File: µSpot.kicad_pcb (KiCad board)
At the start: 2 copper layers, 80 x 35 mm, 54 parts, among them J1 Conn_01x03, Q1 PSMN0R9-30YLD, Q2 PSMN0R9-30YLD, Q3 PSMN0R9-30YLD, Q4 PSMN0R9-30YLD, Q5 PSMN0R9-30YLD, Q6 PSMN0R9-30YLD, SW1 Rotary_Encoder_Switch, U1 AP65211A, U2 MIC5365-3.3YD5, U3 ATtiny406-S, U4 OLED_Display_9616, U5 FAN3111

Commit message: Layout finish
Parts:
- removed C10, C11: 1u, Capacitor_SMD:C_1206_3216Metric_Pad1.42x1.75mm_HandSolder
- added D1: Red, LED_SMD:LED_0805_2012Metric_Pad1.15x1.40mm_HandSolder, F.Cu at (145.7, 91.9)
- added D2: 2SS100L-W, Diode_SMD:D_SOD-123F, F.Cu at (147.6, 109.3)
- added D6: BZX84C3V3, Package_TO_SOT_SMD:SOT-23, F.Cu at (136.7, 90.3)
- added D7: BZX84C3V3, Package_TO_SOT_SMD:SOT-23, F.Cu at (141.0, 97.3)
- added J2: Conn_01x04, Connector_PinSocket_2.54mm:PinSocket_1x04_P2.54mm_Vertical_SMD_Pin1Left, F.Cu at (153.7, 85.7)
- added Q7: Q_PMOS_DGS, Package_TO_SOT_SMD:SOT-23, F.Cu at (149.0, 106.2)
- added R14: 5k, Resistor_SMD:R_0805_2012Metric_Pad1.15x1.40mm_HandSolder, F.Cu at (133.7, 92.3)
- added R22: 1k8, Resistor_SMD:R_0805_2012Metric_Pad1.15x1.40mm_HandSolder, F.Cu at (136.7, 93.2)
- added R23: 5k, Resistor_SMD:R_0805_2012Metric_Pad1.15x1.40mm_HandSolder, F.Cu at (138.0, 99.2)
- added R24: 1k8, Resistor_SMD:R_0805_2012Metric_Pad1.15x1.40mm_HandSolder, F.Cu at (141.1, 100.0)
- C1, C5: footprint Capacitor_SMD:C_1206_3216Metric_Pad1.42x1.75mm_HandSolder -> Capacitor_SMD:C_0805_2012Metric_Pad1.18x1.45mm_HandSolder
- C12, C2, C3, C4, C6: footprint Capacitor_SMD:C_1206_3216Metric_Pad1.42x1.75mm_HandSolder -> Capacitor_SMD:C_0805_2012Metric_Pad1.15x1.40mm_HandSolder
- C7, C8: value 1u -> 1n; footprint Capacitor_SMD:C_1206_3216Metric_Pad1.42x1.75mm_HandSolder -> Capacitor_SMD:C_0805_2012Metric_Pad1.15x1.40mm_HandSolder
- C9: value 1u -> 3.3u; footprint Capacitor_SMD:C_1206_3216Metric_Pad1.42x1.75mm_HandSolder -> Capacitor_SMD:C_0805_2012Metric_Pad1.15x1.40mm_HandSolder
- D3, D4: footprint LED_SMD:LED_1206_3216Metric_Pad1.42x1.75mm_HandSolder -> LED_SMD:LED_0805_2012Metric_Pad1.15x1.40mm_HandSolder
- L1: footprint Inductor_SMD:L_Taiyo-Yuden_MD-2020 -> Inductor_SMD:L_0805_2012Metric_Pad1.15x1.40mm_HandSolder
- R1, R3: value 4k7 -> 10k; footprint Resistor_SMD:R_1206_3216Metric_Pad1.42x1.75mm_HandSolder -> Resistor_SMD:R_0805_2012Metric_Pad1.15x1.40mm_HandSolder
- R10: value 390k -> 10k; footprint Resistor_SMD:R_1206_3216Metric_Pad1.42x1.75mm_HandSolder -> Resistor_SMD:R_0805_2012Metric_Pad1.15x1.40mm_HandSolder
- R11: value 10k -> 100k; footprint Resistor_SMD:R_1206_3216Metric_Pad1.42x1.75mm_HandSolder -> Resistor_SMD:R_0805_2012Metric_Pad1.20x1.40mm_HandSolder
- R12: value 10k -> 5k; footprint Resistor_SMD:R_1206_3216Metric_Pad1.42x1.75mm_HandSolder -> Resistor_SMD:R_0805_2012Metric_Pad1.15x1.40mm_HandSolder
- R13, R15, R16, R17, R18, R19, R2, R20, R21, R4, R5, R6, R7, R8, R9, TH1: footprint Resistor_SMD:R_1206_3216Metric_Pad1.42x1.75mm_HandSolder -> Resistor_SMD:R_0805_2012Metric_Pad1.15x1.40mm_HandSolder
- U1: value AP65211A -> AP65111AWU; footprint Package_TO_SOT_SMD:TSOT-23-6_HandSoldering -> Package_TO_SOT_SMD:TSOT-23-6
- U3: value ATtiny406-S -> ATtiny404-SS; footprint Package_SO:SOIC-20W_7.5x12.8mm_P1.27mm -> Package_SO:SOIC-14_3.9x8.7mm_P1.27mm
- U4: value OLED_Display_9616 -> FAN3111E; footprint µSpot:OLED_Display_9616 -> Package_TO_SOT_SMD:SOT-23-5_HandSoldering
- U5: value FAN3111 -> ADS7029; footprint Package_TO_SOT_SMD:SOT-23-5_HandSoldering -> Package_SO:VSSOP-8_2.3x2mm_P0.5mm
- moved U4 40.5 mm to (108.5, 83.0)
- moved R12 31.4 mm to (164.3, 92.1)
- moved U5 31.2 mm to (134.0, 101.0)
- moved C12 30.7 mm to (166.4, 92.1)
- moved D5 30.7 mm to (171.9, 91.6)
- moved R13 30.7 mm to (168.9, 92.1)
- moved R11 25.0 mm to (143.8, 107.0), turned to 90 degrees
- moved C8 23.6 mm to (141.1, 102.1), turned to 0 degrees
- moved C7 22.6 mm to (136.7, 95.2), turned to 0 degrees
- moved C9 19.6 mm to (134.0, 97.6), turned to 0 degrees
- moved D4 18.4 mm to (141.5, 91.9), turned to 90 degrees
- moved R3 17.1 mm to (143.6, 91.9), turned to 90 degrees
- moved R10 16.3 mm to (157.3, 99.2)
- moved R8 8.84 mm to (129.7, 108.1), turned to 90 degrees
- moved C2 7.93 mm to (150.4, 101.6)
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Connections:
- C5 pad 1: +5V -> +5VA
- C7 pad 1: GND -> /WELD+
- C7 pad 2: Net-(C7-Pad2) -> GND
- C8 pad 1: GND -> /WELD-
- C8 pad 2: Net-(C8-Pad2) -> GND
- C9 pad 1: Net-(C9-Pad1) -> +3V3
- C9 pad 2: Net-(C9-Pad2) -> GND
- J1 pad 1: UDPI -> GND
- J1 pad 2: GND -> /UDPI
- J1 pad 3: +5V -> +5VP
- L1 pad 2: +5V -> +5VA
- R1 pad 1: ON_LED -> /TRIGGER
- R10 pad 1: Net-(R10-Pad1) -> +5VA
- R10 pad 2: GND -> Net-(D1-Pad2)
- R11 pad 1: +3V3 -> +5VP
- R11 pad 2: Net-(R11-Pad2) -> GND
- R4 pad 1: +5V -> +5VA
- R6 pad 2: CLK -> /CLK
- R7 pad 2: DT -> /DT
- R8 pad 2: SDA -> /SCL
- R9 pad 2: SCL -> /SDA
- SW1 pad A: CLK -> /CLK
- SW1 pad B: DT -> /DT
- SW1 pad S1: SWITCH -> /SWITCH
- U1 pad 1: GND -> +BATT
- U1 pad 2: (no net) -> GND
- U1 pad 3: +BATT -> Net-(C4-Pad2)
- U1 pad 4: Net-(R2-Pad2) -> Net-(C4-Pad1)
- U1 pad 6: Net-(C4-Pad1) -> Net-(R2-Pad2)
- U3 pad 10: SDA -> /UDPI
- U3 pad 11: SCL -> /WELD_CS
- U3 pad 12: Net-(U3-Pad12) -> /WELD_ADC
- U3 pad 13: Net-(U3-Pad13) -> /SCLK
- U3 pad 14: Net-(U3-Pad14) -> GND
- U3 pad 2: /TRIGGER -> /BAT_VOL
- U3 pad 3: ON_LED -> /TEMP
- U3 pad 4: Net-(U3-Pad4) -> /TRIGGER
- U3 pad 5: Net-(U3-Pad5) -> /SWITCH
- U3 pad 6: /TEMP -> /CLK
- U3 pad 7: SWITCH -> /DT
- U3 pad 8: CLK -> /SDA
- U3 pad 9: DT -> /SCL
- U4 pad 1: Net-(C9-Pad1) -> +5V
- U4 pad 2: Net-(C9-Pad2) -> GND
- U4 pad 3: Net-(C11-Pad1) -> /TRIGGER
- U4 pad 4: Net-(C11-Pad2) -> GND
- U4 pad 5: +3V3 -> /Welding/G
- U5 pad 1: +5V -> Net-(U5-Pad1)
- U5 pad 2: GND -> /SCLK
- U5 pad 3: /TRIGGER -> /WELD_ADC
- U5 pad 4: GND -> /WELD_CS
- U5 pad 5: /Welding/G -> /WELD-
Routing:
- net +5V: track 148.3 -> 94.5 mm, vias 2 -> 0
- net /SDA: track 0.00 -> 53.1 mm
- net /BAT_VOL: track 20.0 -> 72.0 mm, vias 0 -> 2
- net SDA: track 48.9 -> 0.00 mm
- net /SCL: track 0.00 -> 48.7 mm
- net SCL: track 48.2 -> 0.00 mm
- net /SWITCH: track 0.00 -> 39.1 mm
- net /CLK: track 0.00 -> 37.3 mm
- net ON_LED: track 30.4 -> 0.00 mm
- net /TRIGGER: track 22.9 -> 53.1 mm
- net SWITCH: track 28.3 -> 0.00 mm
- net +5VA: track 0.00 -> 26.8 mm
- net /DT: track 0.00 -> 26.6 mm
- net +5VP: track 0.00 -> 24.1 mm, vias 0 -> 2
- net CLK: track 22.4 -> 0.00 mm
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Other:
- board text added: "JLCJLCJLC"
- board text added: "Negative"
- board text added: "Positive"
- board text added: "Viking Elabs"

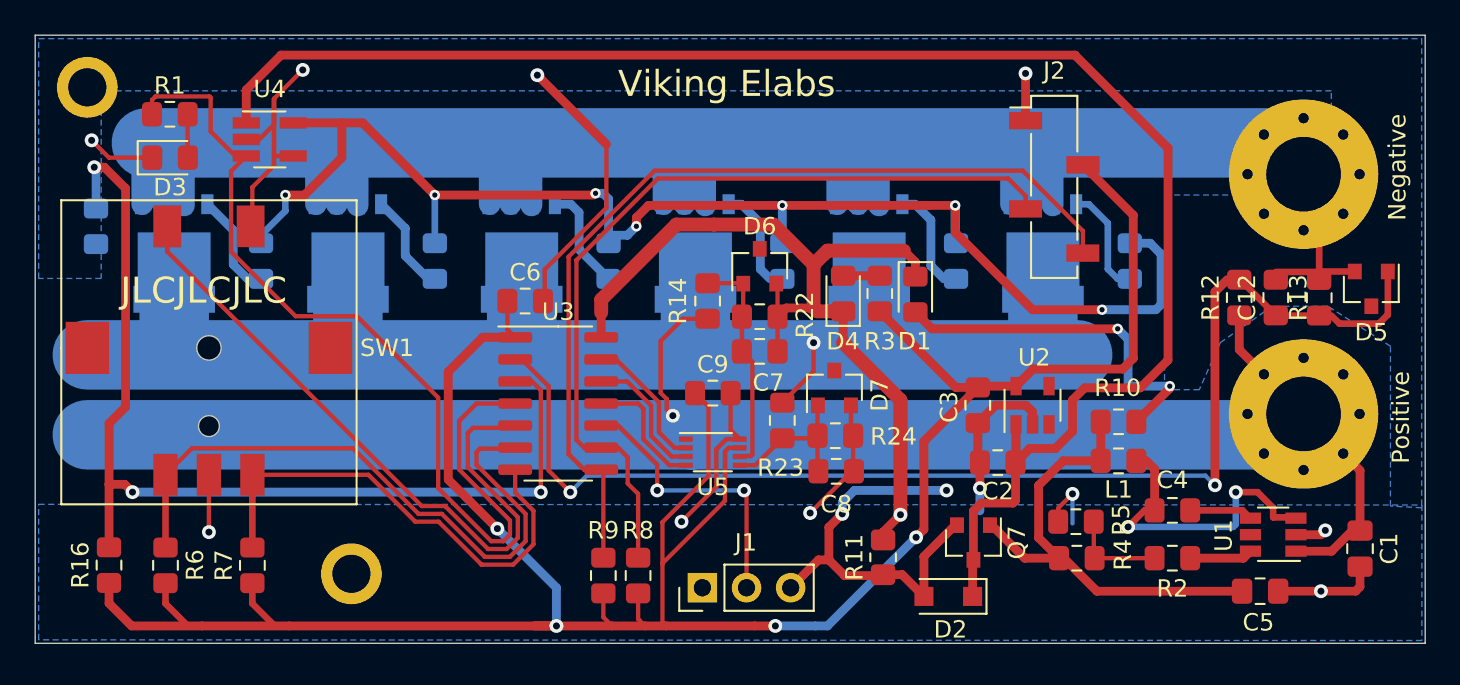
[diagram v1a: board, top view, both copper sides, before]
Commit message: Changes FAN3111 footprint and removed 5V
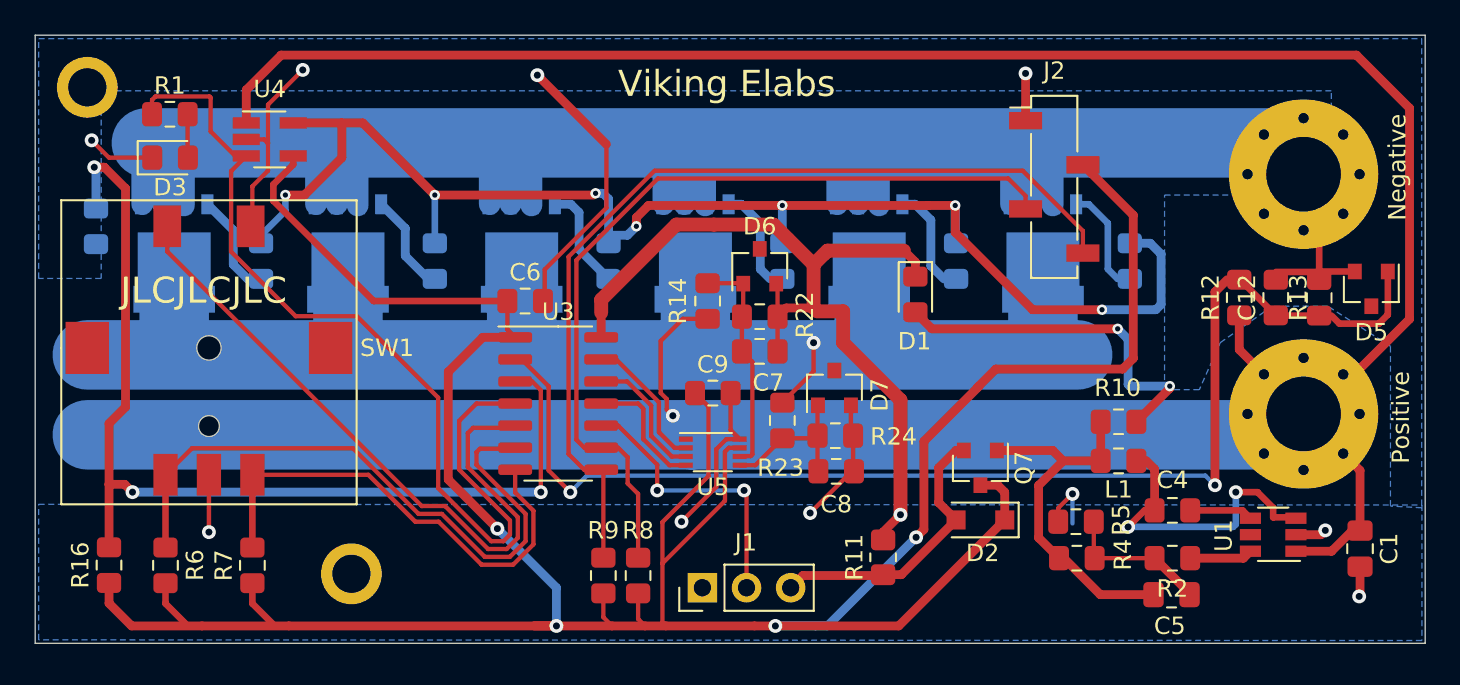
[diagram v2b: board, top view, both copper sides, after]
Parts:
- removed C2, C3: 1uF, Capacitor_SMD:C_0805_2012Metric_Pad1.15x1.40mm_HandSolder
- removed D4: Green, LED_SMD:LED_0805_2012Metric_Pad1.15x1.40mm_HandSolder
- removed R3: 10k, Resistor_SMD:R_0805_2012Metric_Pad1.15x1.40mm_HandSolder
- removed U2: MIC5365-3.3YD5, Package_TO_SOT_SMD:SOT-23-5
- L1: value 6.8u -> 6.5u
- R5: value 7.68k -> 13k
- moved C5 5.10 mm to (160.4, 109.2)
- moved D2 4.77 mm to (149.4, 104.9)
- moved Q7 4.32 mm to (149.4, 101.9)
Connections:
- net +5VA renamed +3.3VA
- net +5VP renamed +3.3VP
- C5 pad 2: GND -> Net-(C5-Pad2)
- D2 pad 1: +5V -> +3V3
- Q7 pad 3: +5V -> +3V3
- R2 pad 1: Net-(R2-Pad1) -> Net-(C5-Pad2)
- R4 pad 2: Net-(R2-Pad1) -> Net-(C5-Pad2)
- R5 pad 1: Net-(R2-Pad1) -> Net-(C5-Pad2)
- U4 pad 1: +5V -> +BATT
- U4 pad 4: GND -> +3V3
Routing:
- net +5V: track 94.5 -> 0.00 mm
- net +BATT: track 97.1 -> 188.6 mm
- net +3V3: track 151.0 -> 181.6 mm
- net GND: track 255.0 -> 236.0 mm, vias 12 -> 11
- net +3.3VP: track 24.1 -> 16.4 mm, vias 2 -> 0
- net Net-(C5-Pad2): track 0.00 -> 7.58 mm
- net +3.3VA: track 26.8 -> 21.5 mm
- net Net-(R2-Pad1): track 4.65 -> 0.00 mm
- net Net-(D4-Pad2): track 2.11 -> 0.00 mm

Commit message: Updated board layout
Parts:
- moved D1 16.7 mm to (161.0, 98.4), turned to 180 degrees
- moved C5 5.53 mm to (165.9, 108.6), turned to 180 degrees
- moved L1 4.86 mm to (162.2, 101.2), turned to 270 degrees
- moved R5 3.56 mm to (157.7, 107.2)
- moved R4 3.46 mm to (157.7, 109.2)
- moved R10 3.28 mm to (159.9, 101.2), turned to 90 degrees
- moved R2 1.76 mm to (162.1, 106.5)
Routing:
- net Net-(D1-Pad2): track 20.8 -> 1.84 mm, vias 2 -> 0
- net +3.3VA: track 21.5 -> 34.5 mm
- net GND: track 236.0 -> 230.7 mm, vias 11 -> 12
- net /BAT_VOL: track 72.0 -> 66.8 mm
- net +3V3: track 181.6 -> 179.5 mm
- net Net-(C5-Pad2): track 7.58 -> 9.38 mm
- net Net-(R2-Pad2): track 3.63 -> 1.90 mm
